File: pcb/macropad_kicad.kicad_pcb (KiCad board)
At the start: 2 copper layers, 81 x 90.5 mm, 28 parts, among them J1 OLED_128x64, SW1 RotaryEncoder_Switch, U1 MOUDLE-SEEEDUINO-XIAO

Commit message: fixed pcb
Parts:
- added G***: LOGO, LOGO, F.Cu at (110.6, 24.4)
- moved U1 2.12 mm to (120.0, 36.2)
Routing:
- net GND: track 61.4 -> 63.5 mm
- net Col 2: track 99.3 -> 101.5 mm
- net +5V: track 38.7 -> 40.8 mm
- net SDA: track 39.5 -> 41.6 mm
- net SCL: track 33.5 -> 35.7 mm
- net Rot B: track 44.8 -> 46.9 mm
- net Rot A: track 51.3 -> 53.4 mm
- net Col 3: track 140.1 -> 142.2 mm
- net Row 2: track 61.2 -> 62.1 mm
- net Row 1: track 95.9 -> 96.7 mm
- net Row 0: track 110.5 -> 111.4 mm
- net Col 1: track 82.1 -> 82.9 mm
- net Col 0: track 77.0 -> 77.9 mm
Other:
- board text added: "@mrdarip"
- board text added: "XIAO HERE!!1!"

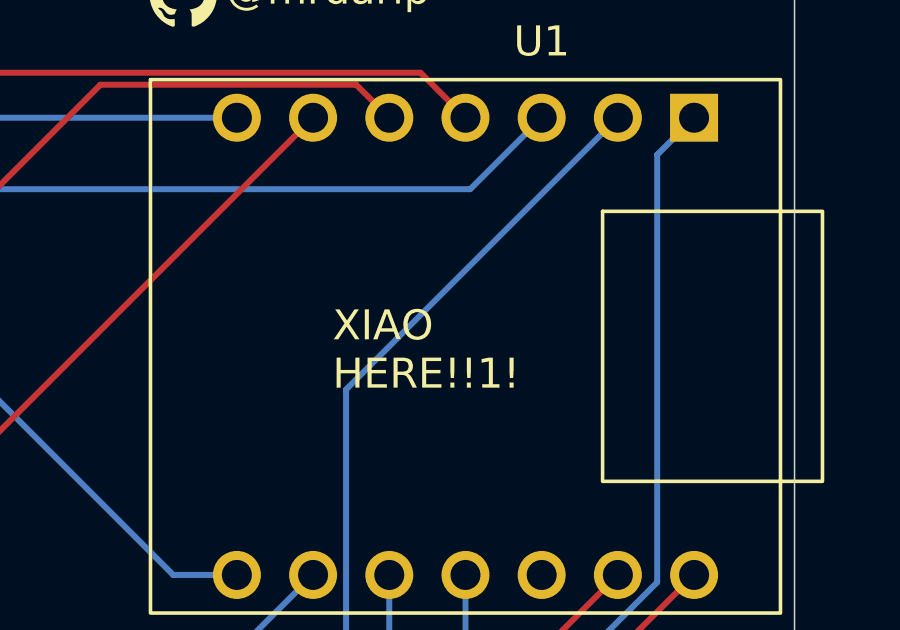
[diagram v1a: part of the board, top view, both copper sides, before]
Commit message: added new silkscreen text and adjusted position of existing text on PCB layout
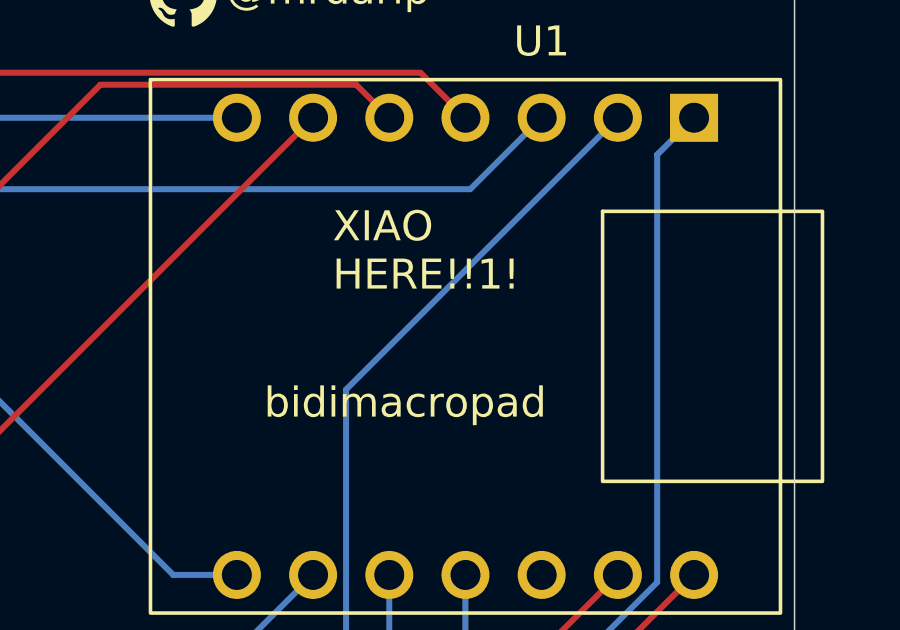
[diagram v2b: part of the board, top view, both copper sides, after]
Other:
- board text added: "bidimacropad"
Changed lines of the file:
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@@
 		(layer "Edge.Cuts")
 	)
-	(gr_text "XIAO\nHERE!!1!"
-		(at 115.57 37.6936 0)
+	(gr_text "bidimacropad"
+		(at 113.284 38.6588 0)
 		(layer "F.SilkS")
 		(effects
+			(font
+				(size 1 1)
+				(thickness 0.1)
+			)
+			(justify left bottom)
+		)
+	)
+	(gr_text "XIAO\nHERE!!1!"
+		(at 115.57 34.3916 0)
+		(layer "F.SilkS")
+		(effects
